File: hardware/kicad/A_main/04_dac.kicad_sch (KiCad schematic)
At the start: 34 parts, among them J30 SMA TX1, J31 SMA TX2, J32 SMA TX3, J33 SMA TX4, T10 ADT1-1WT+, T11 ADT1-1WT+, T12 ADT1-1WT+, T13 ADT1-1WT+, U10 LFE5U-25F-7BG256I, U30 AD9767ASTZ, U31 AD9767ASTZ

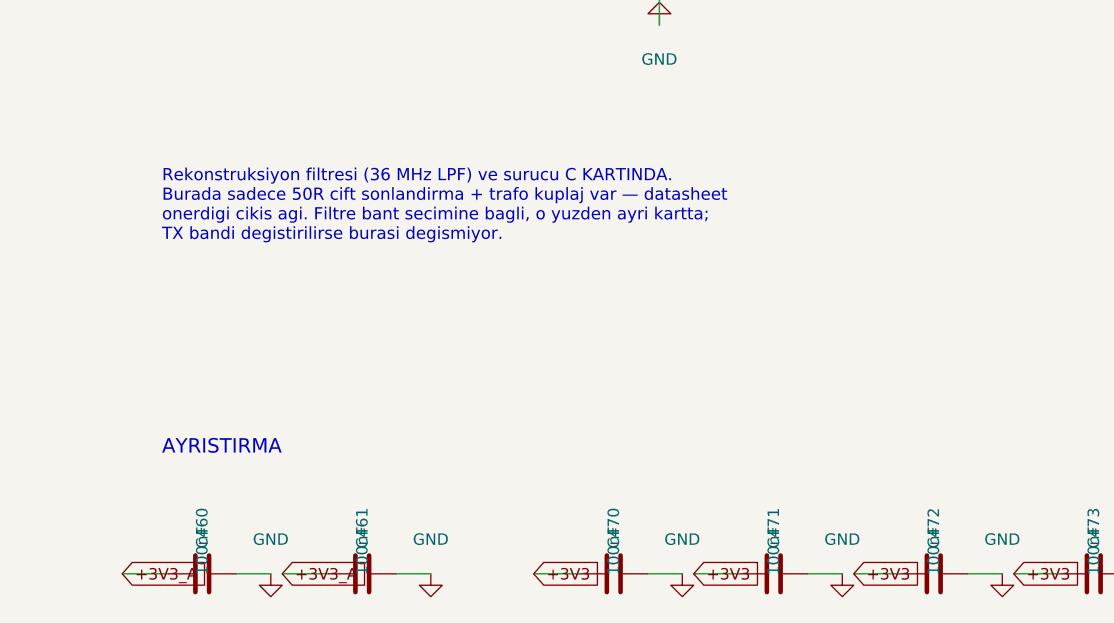
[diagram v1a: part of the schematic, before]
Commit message: Correct the transmit envelope and add a third zero on 15 m to 10 m
The unit has no reconstruction filter. A comment on board A said that
the filter is on board C. Board C has no such filter: the transmit
signal enters through an SMA connector and goes to the transmit and
receive relay. The datasheet also gave a cutoff frequency for this
filter that does not exist.

A sampling DAC does not make one frequency. It makes images at
|k*fs +/- fd|. The zero-order hold gives each image a different
level, and the function falls slowly. If the carrier is near Nyquist,
an image at a lower frequency can be stronger than the carrier.

A new tool measures this. It uses the harmonic filter of board D,
because that filter is the only one in the transmit path.

  15 m to 10 m   4-channel   image at 10.3 MHz is 10.4 dB stronger
  6 m            4-channel   image is 14.2 dB stronger
  6 m            2-channel   image is 7.4 dB stronger
  20 m, 17 m     4-channel   -12.0 dBc, the limit is -43 dBc
  15 m to 10 m   2-channel   -40.4 dBc, the limit is -43 dBc

Only the last one is correctable.

That filter position must attenuate three frequencies: 42 MHz (the
second harmonic of 21 MHz), 63 MHz (the third harmonic) and 50.3 MHz
(the DAC image). A five-pole filter has two traps. No pair of trap
frequencies gives more than 1.9 dB of margin, and 1.9 dB is not a
margin: one E24 rounding already cost 19 dB in this project.

A shunt series-LC at the output adds a third zero. The image goes
from -40.4 dBc to -47.3 dBc, and the margin becomes 23 dB. Above
resonance the branch is capacitive and attenuates the whole stopband,
so the harmonics also improve. The passband loss falls from 1.35 dB
to 0.99 dB.

The transmit envelope is now written honestly. The RTL said "Nyquist
is 20 MHz, so 160 m to 17 m". Nyquist alone is not enough: the images
must also be filtered, and the real limit is lower.

  4-channel   160 m to 30 m
  2-channel   160 m to 10 m
  6 m         no transmit. Receive works, with 68 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
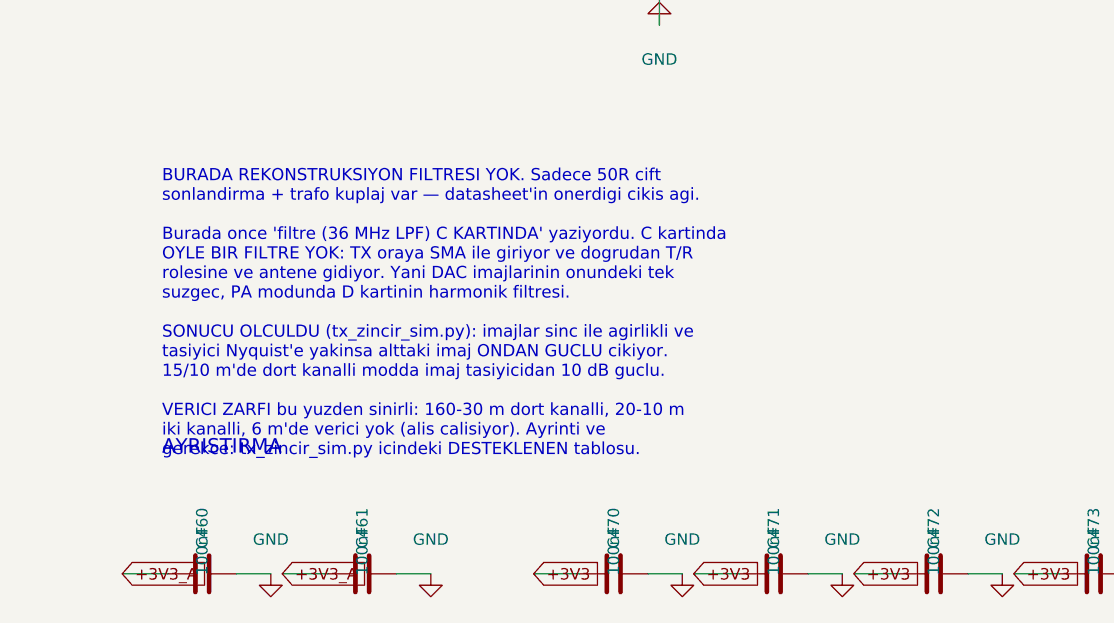
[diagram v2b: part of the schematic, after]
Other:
- note added: "BURADA REKONSTRUKSIYON FILTRESI YOK. Sadece 50R cift sonlandirma + trafo kuplaj var — datasheet'in onerdigi cikis agi. Burada once 'filtre (36 MHz LPF) C KARTINDA' yaziyordu. C kartinda OYLE BIR FILTRE YOK: TX oraya SMA ile giriyor ve dogrudan T/R rolesine ve antene gidiyor. Yani DAC imajlarinin onundeki tek suzgec, PA modunda D kartinin harmonik filtresi. SONUCU OLCULDU (tx_zincir_sim.py): imajl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"
- note removed: "Rekonstruksiyon filtresi (36 MHz LPF) ve surucu C KARTINDA. Burada sadece 50R cift sonlandirma + trafo kuplaj var — datasheet onerdigi cikis agi. Filtre bant secimine bagli, o yuzden ayri kartta; TX bandi degistirilirse burasi degismiyor."
